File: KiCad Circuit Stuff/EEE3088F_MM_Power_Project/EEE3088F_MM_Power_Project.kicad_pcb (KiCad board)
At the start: 2 copper layers, 77.3 x 58.5 mm, 88 parts, among them J1 Conn_01x02, J2 Conn_02x16_Odd_Even, U1 MT3608, U10 DRV8833PWP, U11 SS-12D06-G050, U12 AP22814AW5-7, U14 AP22814AW5-7, U2 INA219AIDCNR, U3 AMS1117-3.3, U4 TPS5430DDAR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

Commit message: Tweaked some stuff
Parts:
- moved C4 1.86 mm to (125.9, 113.2)
- moved U3 1.30 mm to (131.2, 114.7)
- moved C5 1.30 mm to (125.3, 117.9)
- moved L3 0.48 mm to (173.1, 125.1)
- moved J1 0.43 mm to (113.7, 146.2)
- moved JP1 0.43 mm to (113.4, 130.0)
- moved U11 0.23 mm to (110.0, 138.5)
- moved R5 0.17 mm to (113.4, 128.0)
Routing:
- net +3V3: track 109.1 -> 107.7 mm
- net /PH_Pin: track 13.1 -> 13.7 mm

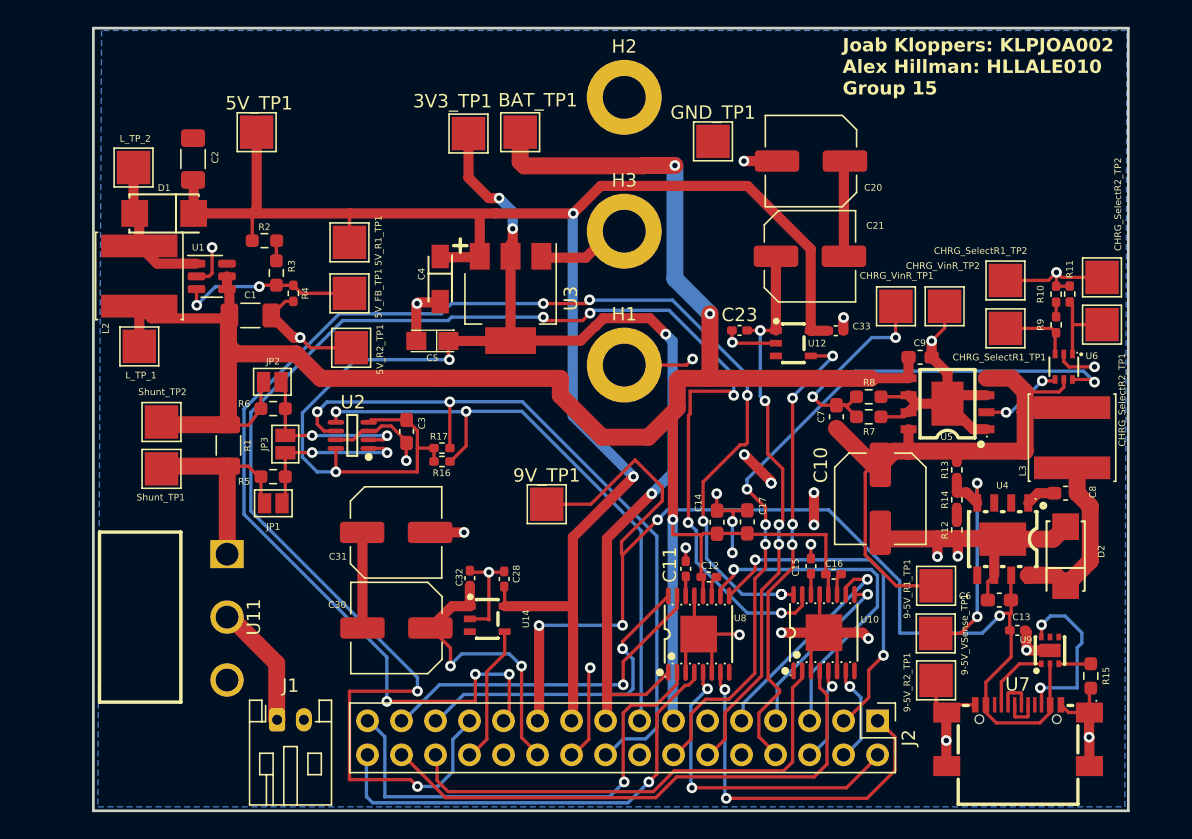
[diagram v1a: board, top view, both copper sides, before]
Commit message: Change silkscreen and drill hole issues
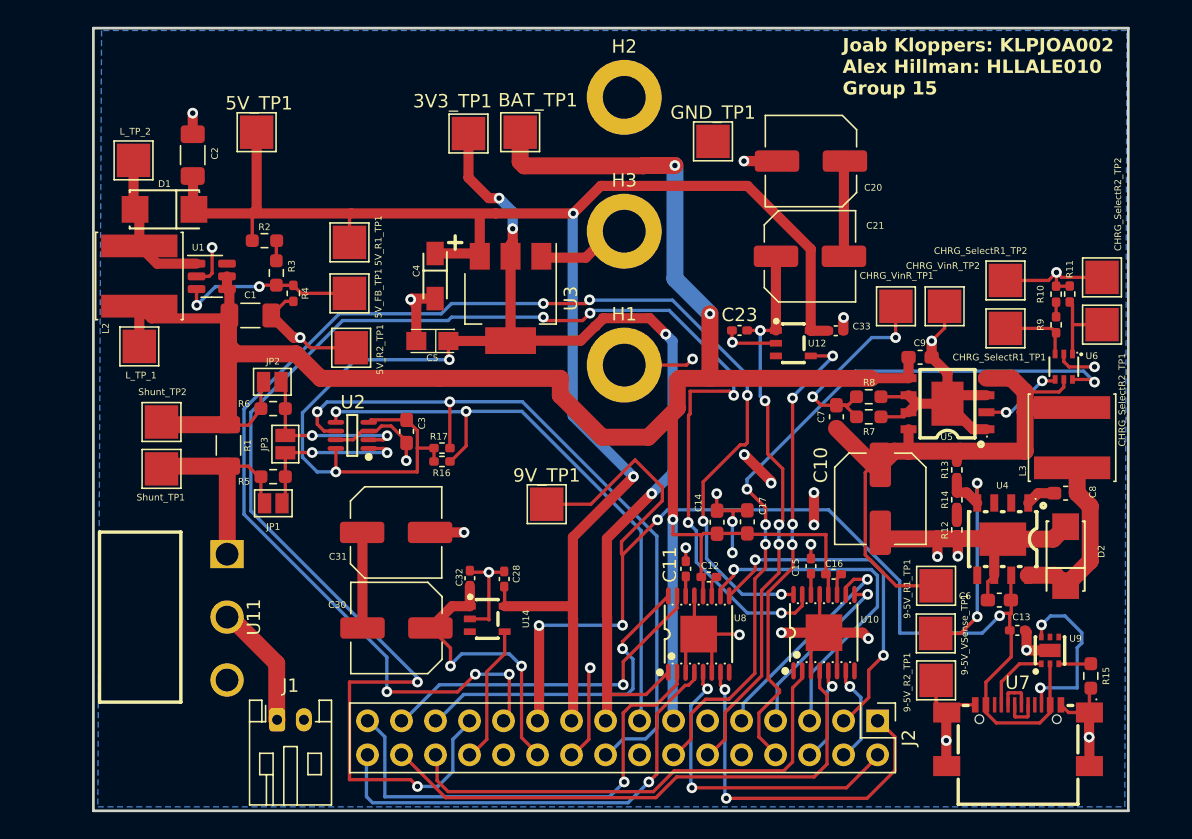
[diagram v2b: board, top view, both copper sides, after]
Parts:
- moved L_TP_2 0.53 mm to (103.0, 104.4)
- moved C4 0.44 mm to (125.5, 113.0)
- moved D1 0.31 mm to (105.3, 108.0)
- moved C2 0.29 mm to (107.4, 104.0)
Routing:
- net GND: track 185.4 -> 187.7 mm
- net /AIN1 (U2): track 107.4 -> 105.2 mm, vias 10 -> 8
- net Net-(D1-A): track 10.9 -> 11.4 mm

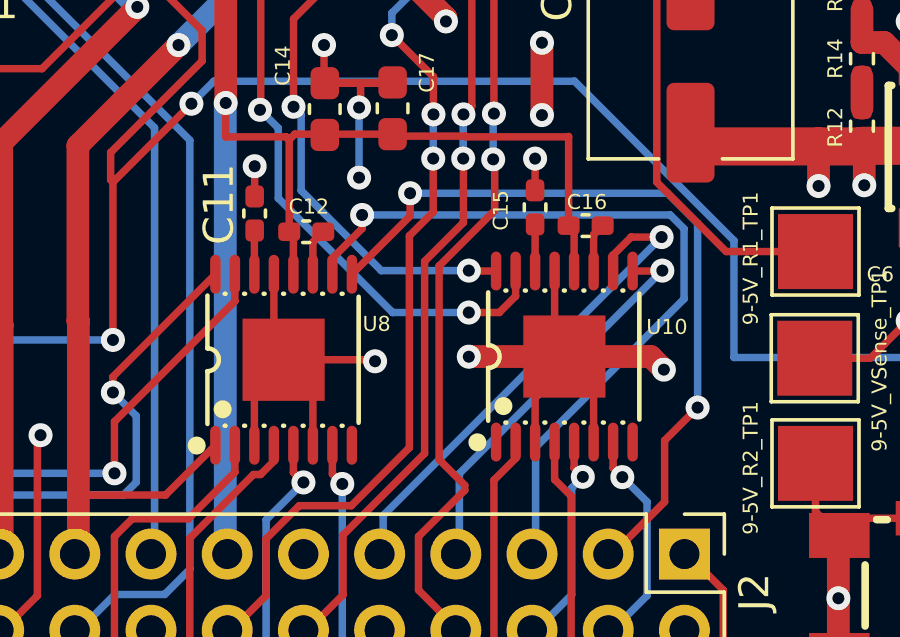
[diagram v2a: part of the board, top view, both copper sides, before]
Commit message: Added some lables in Joab Schematic
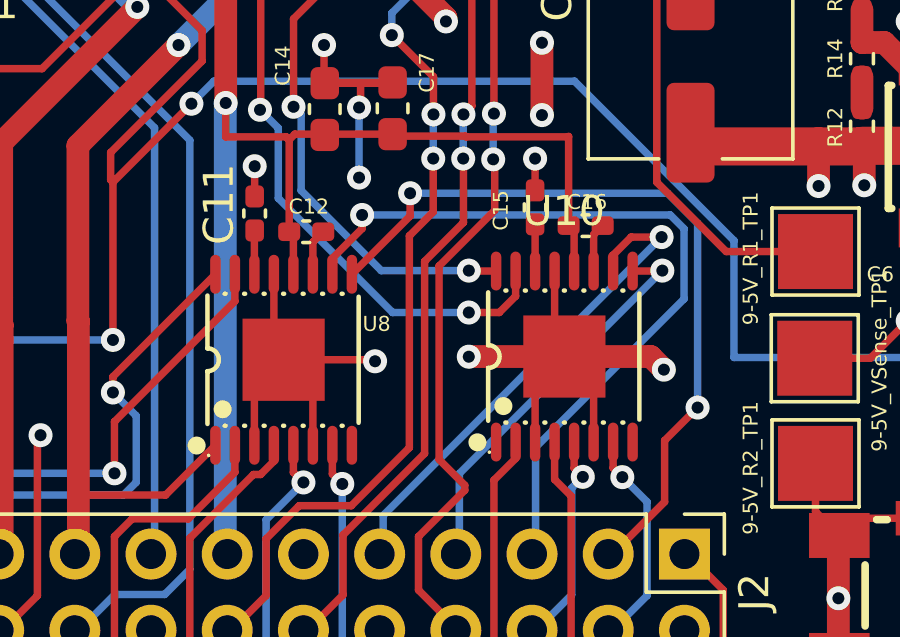
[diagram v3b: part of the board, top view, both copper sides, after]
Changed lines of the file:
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@@
     (fp_circle (center -2.898908 2.859538) (end -2.748793 2.859538)
       (stroke (width 0.3) (type solid)) (fill none) (layer "F.SilkS"))
+    (fp_circle (center -2.499873 3.187452) (end -2.469901 3.187452)
+      (stroke (width 0.059995) (type solid)) (fill none) (layer "F.SilkS"))
     (fp_circle (center -2.032004 1.651003) (end -1.88189 1.651003)
       (stroke (width 0.3) (type solid)) (fill none) (layer "F.SilkS"))
@@
       (net 4 "GND") (pinfunction "GND") (pintype "unspecified"))
     (model "packages3d/TSSOP-16_L5.0-W4.4-P0.65-LS6.4-BL-EP.step"
-      (offset (xyz -914.5387973 686.1865777 0))
+      (offset (xyz -0 0 0))
       (scale (xyz 1 1 1))
       (rotate (xyz 0 0 -90))
@@
     (property "ki_keywords" "C50506")
     (attr smd)
-    (fp_text reference "U10" (at 3.418083 -0.985387) (layer "F.SilkS")
-        (effects (font (size 0.5 0.5) (thickness 0.125)))
+    (fp_text reference "U10" (at -0.020003 -4.850013) (layer "F.SilkS")
+        (effects (font (size 1 1) (thickness 0.15)))
     )
     (fp_text value "DRV8833PWP" (at -0.020003 4.850013) (layer "F.Fab")
@@
     (fp_circle (center -2.898908 2.859538) (end -2.748793 2.859538)
       (stroke (width 0.3) (type solid)) (fill none) (layer "F.SilkS"))
+    (fp_circle (center -2.499873 3.187452) (end -2.469901 3.187452)
+      (stroke (width 0.059995) (type solid)) (fill none) (layer "F.SilkS"))
     (fp_circle (center -2.032004 1.651003) (end -1.88189 1.651003)
       (stroke (width 0.3) (type solid)) (fill none) (layer "F.SilkS"))
@@
       (net 4 "GND") (pinfunction "GND") (pintype "unspecified"))
     (model "packages3d/TSSOP-16_L5.0-W4.4-P0.65-LS6.4-BL-EP.step"
-      (offset (xyz -914.5387973 686.1865777 0))
+      (offset (xyz -0 0 0))
       (scale (xyz 1 1 1))
       (rotate (xyz 0 0 -90))
